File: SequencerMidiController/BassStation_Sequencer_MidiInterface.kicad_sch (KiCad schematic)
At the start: 0 parts

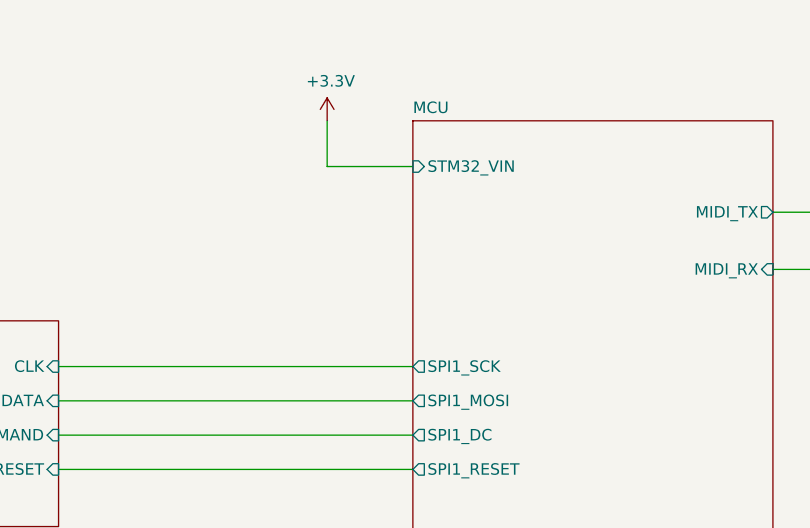
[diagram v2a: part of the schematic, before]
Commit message: Checked microSD card connector pins and added board layout connector footprint
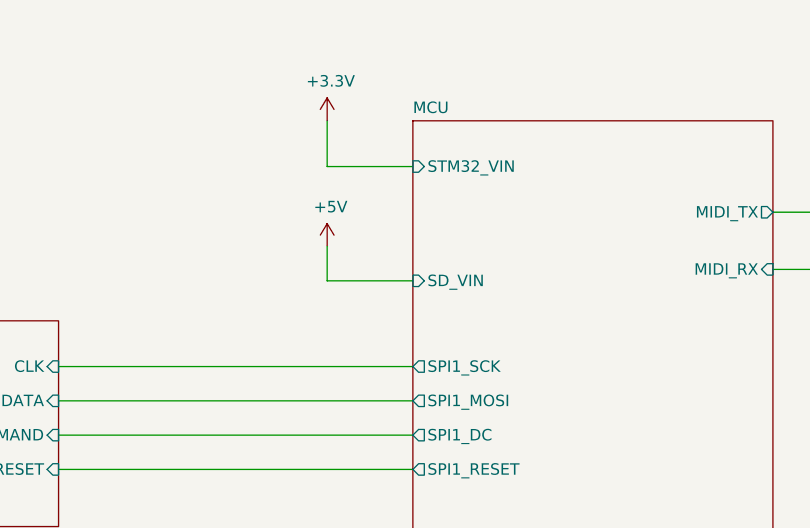
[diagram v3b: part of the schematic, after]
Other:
- sheet MCU ports: added SD_VIN; removed none
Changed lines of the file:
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@@
+    (stroke (width 0) (type default) (color 0 0 0 0))
+  )
+  (wire (pts (xy 210.185 98.425) (xy 200.66 98.425))
+    (stroke (width 0) (type default) (color 0 0 0 0))
+  )
+  (wire (pts (xy 200.66 98.425) (xy 200.66 94.615))
     (stroke (width 0) (type default) (color 0 0 0 0))
   )
@@
     )
     (property "Datasheet" "" (id 3) (at 103.505 74.93 0)
+      (effects (font (size 1.27 1.27)) hide)
+    )
+    (pin "1")
+  )
+  (symbol (lib_id "power:+5V") (at 200.66 94.615 0) (unit 1)
+    (in_bom yes) (on_board yes)
+    (property "Reference" "#PWR0112" (id 0) (at 200.66 98.425 0)
+      (effects (font (size 1.27 1.27)) hide)
+    )
+    (property "Value" "+5V" (id 1) (at 201.041 90.2208 0))
+    (property "Footprint" "" (id 2) (at 200.66 94.615 0)
+      (effects (font (size 1.27 1.27)) hide)
+    )
+    (property "Datasheet" "" (id 3) (at 200.66 94.615 0)
       (effects (font (size 1.27 1.27)) hide)
     )
@@
     )
     (pin "I2C3_INT" output (at 210.185 178.435 180)
+      (effects (font (size 1.27 1.27)) (justify left))
+    )
+    (pin "SD_VIN" input (at 210.185 98.425 180)
       (effects (font (size 1.27 1.27)) (justify left))
     )
@@
     (path "/00000000-0000-0000-0000-000060bd3123/00000000-0000-0000-0000-000063615dfb" (page "45"))
     (path "/00000000-0000-0000-0000-000060bd3123/00000000-0000-0000-0000-000060bd5aa5" (page "46"))
+    (path "/00000000-0000-0000-0000-000060bcdcf5/51a02b96-021c-4b48-afb3-b2c25e2d9e78" (page "47"))
   )
   (symbol_instances
@@
       (reference "#PWR0111") (unit 1) (value "GNDS") (footprint "")
     )
+    (path "/85830388-c34d-4f3f-a78d-9eed77152365"
+      (reference "#PWR0112") (unit 1) (value "+5V") (footprint "")
+    )
+    (path "/00000000-0000-0000-0000-000060bcdcf5/51a02b96-021c-4b48-afb3-b2c25e2d9e78/30bbb9d6-605e-4200-8ccb-d7b5ec008bc2"
+      (reference "#PWR0113") (unit 1) (value "GNDS") (footprint "")
+    )
     (path "/00000000-0000-0000-0000-000060bd3123/00000000-0000-0000-0000-000060bd5aa5/00000000-0000-0000-0000-000060bd6867"
       (reference "C1") (unit 1) (value "10uF 20V X5R") (footprint "Resistor_SMD:R_1206_3216Metric_Pad1.30x1.75mm_HandSolder")
@@
     )
     (path "/00000000-0000-0000-0000-000060bd3123/00000000-0000-0000-0000-000060bd33f0/00000000-0000-0000-0000-000060b71c00"
-      (reference "D1") (unit 1) (value "MMSZ4694T1G") (footprint "Diode_SMD:D_SOD-123")
+      (reference "D1") (unit 1) (value "MMSZ4694T1G") (footprint "Diode_SMD:D_SOD-123F")
     )
     (path "/00000000-0000-0000-0000-000060b3fce7/00000000-0000-0000-0000-000060b99aa1"
@@
       (reference "J2") (unit 1) (value "MIDI OUT") (footprint "RS_5P180_DIN5_SOCKET_WSHIELD:RS_5P180_DIN5_SOCKET_WSHIELD")
     )
+    (path "/00000000-0000-0000-0000-000060bcdcf5/51a02b96-021c-4b48-afb3-b2c25e2d9e78/6a7300ee-6e79-40d6-b10b-d01417e45e41"
+      (reference "J3") (unit 1) (value "Conn_01x06") (footprint "Connector_PinSocket_2.54mm:PinSocket_1x06_P2.54mm_Horizontal")
+    )
     (path "/00000000-0000-0000-0000-000060bcddb1/00000000-0000-0000-0000-000060c5e3d9"
